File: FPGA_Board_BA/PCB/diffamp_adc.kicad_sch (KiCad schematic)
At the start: 12 parts, among them U1601 1819_IS8

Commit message: work
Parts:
- renumbered C1601 to C28, C1604 to C29, C1606 to C30, C1607 to C31, C1608 to C32, R1601 to R16, R1603 to R17, R1605 to R18, R1607 to R19, R1608 to R20, R1609 to R21, U1601 to U8

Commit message: 18.11 Bib Session
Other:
- moved on the sheet: C32, U8C
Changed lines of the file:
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@@
 	)
 	(junction
-		(at 199.39 90.17)
+		(at 218.44 90.17)
 		(diameter 0)
 		(color 0 0 0 0)
@@
 	)
 	(junction
-		(at 199.39 115.57)
+		(at 218.44 115.57)
 		(diameter 0)
 		(color 0 0 0 0)
@@
 	(wire
 		(pts
-			(xy 204.47 93.98) (xy 204.47 90.17)
+			(xy 223.52 93.98) (xy 223.52 90.17)
 		)
 		(stroke
@@
 	(wire
 		(pts
-			(xy 199.39 115.57) (xy 199.39 119.38)
+			(xy 218.44 115.57) (xy 218.44 119.38)
 		)
 		(stroke
@@
 	(wire
 		(pts
-			(xy 194.31 105.41) (xy 194.31 115.57)
+			(xy 213.36 105.41) (xy 213.36 115.57)
 		)
 		(stroke
@@
 	(wire
 		(pts
-			(xy 199.39 115.57) (xy 204.47 115.57)
+			(xy 218.44 115.57) (xy 223.52 115.57)
 		)
 		(stroke
@@
 	(wire
 		(pts
-			(xy 194.31 90.17) (xy 194.31 97.79)
+			(xy 213.36 90.17) (xy 213.36 97.79)
 		)
 		(stroke
@@
 	(wire
 		(pts
-			(xy 199.39 86.36) (xy 199.39 90.17)
+			(xy 218.44 86.36) (xy 218.44 90.17)
 		)
 		(stroke
@@
 	(wire
 		(pts
-			(xy 199.39 90.17) (xy 194.31 90.17)
+			(xy 218.44 90.17) (xy 213.36 90.17)
 		)
 		(stroke
@@
 	(wire
 		(pts
-			(xy 204.47 90.17) (xy 199.39 90.17)
+			(xy 223.52 90.17) (xy 218.44 90.17)
 		)
 		(stroke
@@
 	(wire
 		(pts
-			(xy 204.47 109.22) (xy 204.47 115.57)
+			(xy 223.52 109.22) (xy 223.52 115.57)
 		)
 		(stroke
@@
 	(wire
 		(pts
-			(xy 194.31 115.57) (xy 199.39 115.57)
+			(xy 213.36 115.57) (xy 218.44 115.57)
 		)
 		(stroke
@@
 	(symbol
 		(lib_id "power:+5VA")
-		(at 199.39 86.36 0)
+		(at 218.44 86.36 0)
 		(unit 1)
 		(exclude_from_sim no)
@@
 		(fields_autoplaced yes)
 		(property "Reference" "#PWR036"
-			(at 199.39 90.17 0)
+			(at 218.44 90.17 0)
 			(effects
 				(font
@@
 		)
 		(property "Value" "+5VA"
-			(at 199.39 81.28 0)
+			(at 218.44 81.28 0)
 			(effects
 				(font
@@
 		)
 		(property "Footprint" ""
-			(at 199.39 86.36 0)
+			(at 218.44 86.36 0)
 			(effects
 				(font
@@
 		)
 		(property "Datasheet" ""
-			(at 199.39 86.36 0)
+			(at 218.44 86.36 0)
 			(effects
 				(font
@@
 		)
 		(property "Description" "Power symbol creates a global label with name \"+5VA\""
-			(at 199.39 86.36 0)
+			(at 218.44 86.36 0)
 			(effects
 				(font
@@
 	(symbol
 		(lib_id "MYLIB_Misc:LT1819_IS8")
-		(at 198.12 101.6 0)
+		(at 217.17 101.6 0)
 		(mirror y)
 		(unit 3)
@@
 		(fields_autoplaced yes)
 		(property "Reference" "U8"
-			(at 205.74 100.3299 0)
+			(at 224.79 100.3299 0)
 			(effects
 				(font
@@
 		)
 		(property "Value" "1819_IS8"
-			(at 205.74 102.8699 0)
+			(at 224.79 102.8699 0)
 			(effects
 				(font
@@
 		)
 		(property "Footprint" "MYLIB_Misc:LT1819"
-			(at 197.866 88.646 0)
+			(at 216.916 88.646 0)
 			(effects
 				(font
@@
 		)
 		(property "Datasheet" "https://www.analog.com/media/en/technical-documentation/data-sheets/18189fb.pdf"
-			(at 198.628 84.074 0)
+			(at 217.678 84.074 0)
 			(effects
 				(font
@@
 		)
 		(property "Description" "ual wide bandwidth, high slew rate, low noise and distortion operational amplifi ers with excellent DC performance"
-			(at 198.374 86.106 0)
+			(at 217.424 86.106 0)
 			(effects
 				(font
@@
 	(symbol
 		(lib_id "WLIB_C:100n_0603")
-		(at 194.31 101.6 0)
+		(at 213.36 101.6 0)
 		(mirror y)
 		(unit 1)
@@
 		(dnp no)
 		(property "Reference" "C32"
-			(at 190.5 100.3299 0)
+			(at 209.55 100.3299 0)
 			(effects
 				(font
@@
 		)
 		(property "Value" "100n_0603"
-			(at 190.5 102.8699 0)
+			(at 209.55 102.8699 0)
 			(effects
 				(font
@@
 		)
 		(property "Footprint" "WLIB_Capacitor:C_0603"
-			(at 194.31 87.63 0)
+			(at 213.36 87.63 0)
 			(effects
 				(font
@@
 		)
 		(property "Datasheet" "https://www.farnell.com/datasheets/2860632.pdf"
-			(at 194.0052 80.01 0)
+			(at 213.0552 80.01 0)
 			(effects
 				(font
@@
 		)
 		(property "Description" "Unpolarized capacitor SMD MLCC"
-			(at 194.31 101.6 0)
+			(at 213.36 101.6 0)
 			(effects
 				(font
@@
 		)
 		(property "FARNELL" "1759037"
-			(at 194.0052 85.09 0)
+			(at 213.0552 85.09 0)
 			(effects
 				(font
@@
 		)
 		(property "VDC" "25V"
-			(at 194.0052 82.55 0)
+			(at 213.0552 82.55 0)
 			(effects
 				(font
@@
 		)
 		(property "JLCPCB" "C2762593"
-			(at 194.31 90.17 0)
+			(at 213.36 90.17 0)
 			(effects
 				(font
@@
 	(symbol
 		(lib_id "power:GND")
-		(at 199.39 119.38 0)
+		(at 218.44 119.38 0)
 		(unit 1)
 		(exclude_from_sim no)
@@
 		(fields_autoplaced yes)
 		(property "Reference" "#PWR037"
-			(at 199.39 125.73 0)
+			(at 218.44 125.73 0)
 			(effects
 				(font
@@
 		)
 		(property "Value" "GND"
-			(at 199.39 124.46 0)
+			(at 218.44 124.46 0)
 			(effects
 				(font
@@
 		)
 		(property "Footprint" ""
-			(at 199.39 119.38 0)
+			(at 218.44 119.38 0)
 			(effects
 				(font
@@
 		)
 		(property "Datasheet" ""
-			(at 199.39 119.38 0)
+			(at 218.44 119.38 0)
 			(effects
 				(font
@@
 		)
 		(property "Description" "Power symbol creates a global label with name \"GND\" , ground"
-			(at 199.39 119.38 0)
+			(at 218.44 119.38 0)
 			(effects
 				(font

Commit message: 22.11
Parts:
- added R206, R208: 9k1_0603, Resistor_SMD:R_0603_1608Metric, symbol WLIB_R:9k1_0603
- added R207: 1k_0603, Resistor_SMD:R_0603_1608Metric, symbol WLIB_R:1k_0603
- renumbered R17 to R10, R18 to R11, R19 to R12, R20 to R13, R21 to R14, R16 to R9, U8 to U4
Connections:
- net +5VA: no longer R14.2
- net Analog: now also R207.1; no longer R13.2, U4.3 (+)
- net GND: now also R206.2, R208.2
- new net: R13.2, R206.1, R207.2, R208.1, U4.3 (+)
- new net REFOUT_1: R14.2
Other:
- note added: "ADC Reference is 4.096V Vout = V * R1 / (R1 + R2) 4.096V = 5V * R1 / (R1 + R2) 0.8192 = R1 / (R1 + R2) 0.8192 * R1 + 0.8192 * R2 = R1 0.1808 * R1 = 0.8192 * R2 R1 / R2 = 4.53097 R1 := 9.1k || 9.1k = 4.55k R2 = 1k R1/R2 = 4.55 Vout_max = 5V * 4.55 / 5.55 = 4.099V -> very little saturation"
- note added: "R1"
- note added: "R2"

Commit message: exported stuff
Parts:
- renumbered R206 to R15, R207 to R16, R208 to R17
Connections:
- net REFOUT_1 renamed REFOUT_M
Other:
- note added: "Single ended to differential for CHB"

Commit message: schematic fixes after Leo Meeting
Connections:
- net at R15.1, R16.2, R17.1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: no longer R13.2
- net at R9.2, U4.1, U4.2 (-): now also R13.2
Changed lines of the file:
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@@
 	)
 	(junction
-		(at 154.94 73.66)
+		(at 138.43 85.09)
 		(diameter 0)
 		(color 0 0 0 0)
@@
 	(wire
 		(pts
-			(xy 129.54 73.66) (xy 154.94 73.66)
-		)
-		(stroke
-			(width 0)
-			(type default)
-		)
-	)
-	(wire
-		(pts
 			(xy 127 143.51) (xy 135.89 143.51)
 		)
@@
 	(wire
 		(pts
+			(xy 138.43 85.09) (xy 154.94 85.09)
+		)
+		(stroke
+			(width 0)
+			(type default)
+		)
+	)
+	(wire
+		(pts
 			(xy 110.49 90.17) (xy 110.49 76.2)
 		)
@@
 	(wire
 		(pts
-			(xy 154.94 73.66) (xy 154.94 109.22)
+			(xy 138.43 85.09) (xy 138.43 90.17)
 		)
 		(stroke
@@
 	(wire
 		(pts
-			(xy 138.43 78.74) (xy 138.43 90.17)
+			(xy 138.43 78.74) (xy 138.43 85.09)
 		)
 		(stroke
@@
 	(wire
 		(pts
+			(xy 154.94 109.22) (xy 154.94 85.09)
+		)
+		(stroke
+			(width 0)
+			(type default)
+		)
+	)
+	(wire
+		(pts
 			(xy 110.49 100.33) (xy 116.84 100.33)
 		)
@@
 	(wire
 		(pts
-			(xy 154.94 73.66) (xy 175.26 73.66)
-		)
-		(stroke
+			(xy 129.54 73.66) (xy 175.26 73.66)
+		)
+		(stroke

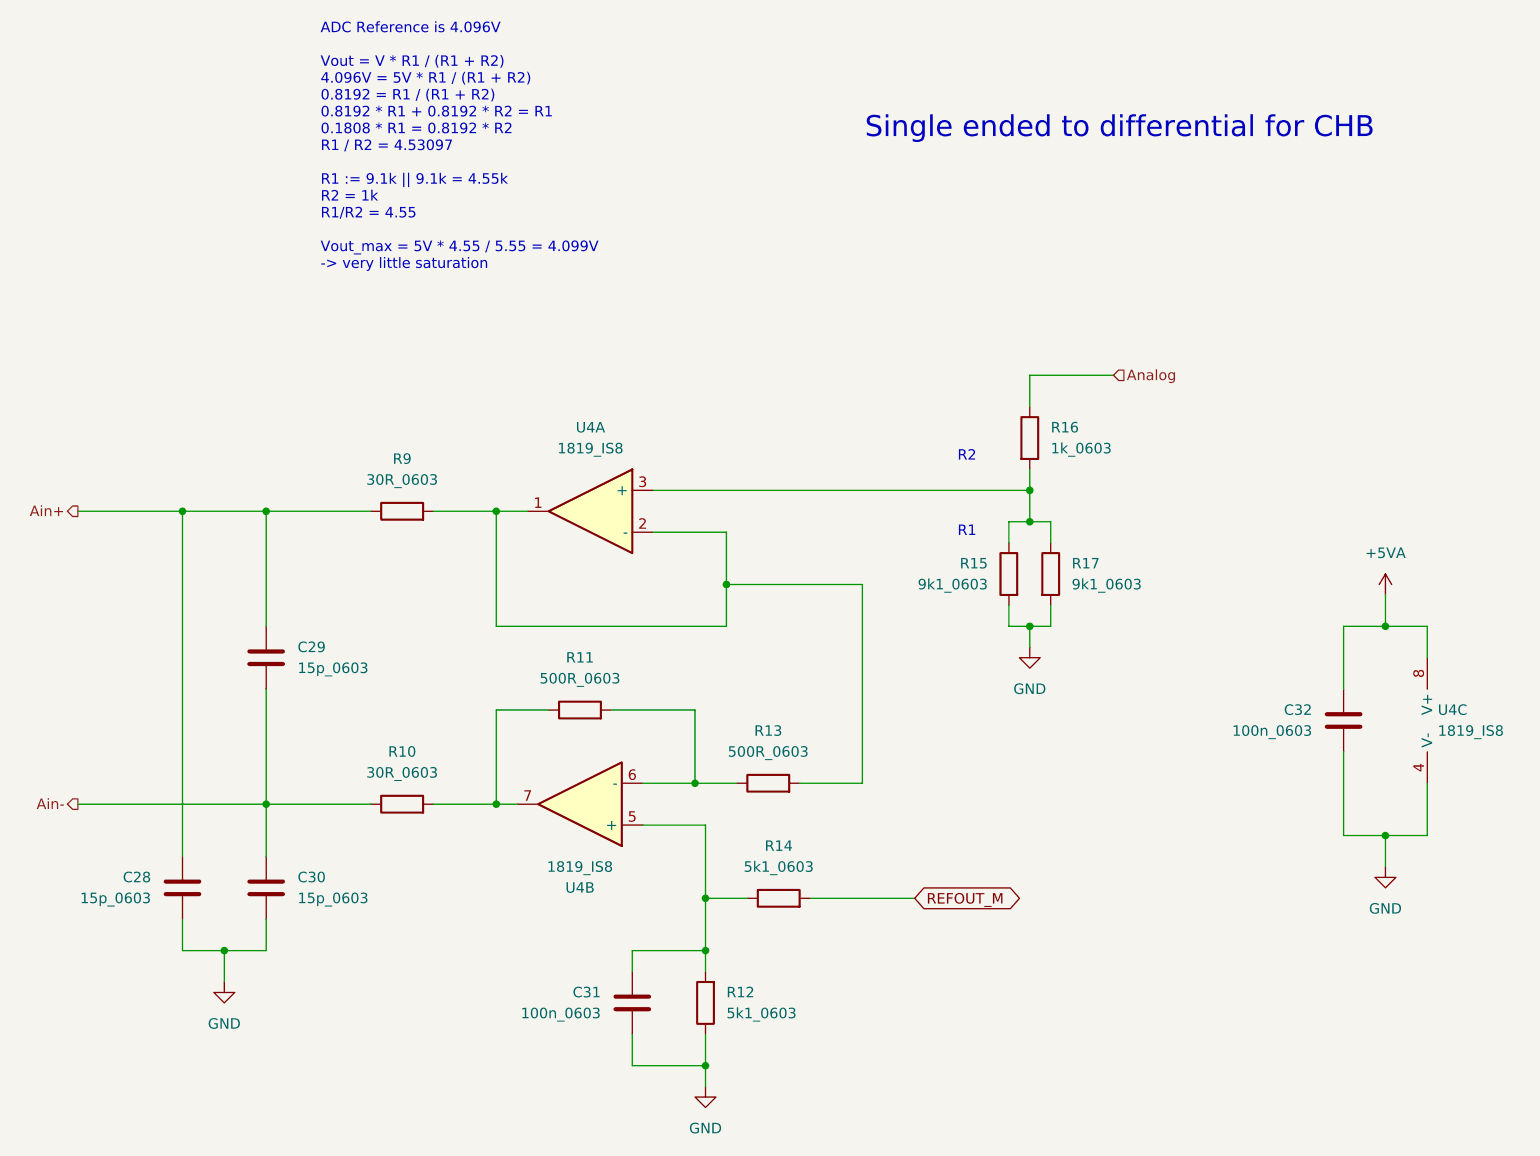
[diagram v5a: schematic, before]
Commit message: component placement with new concept is ready
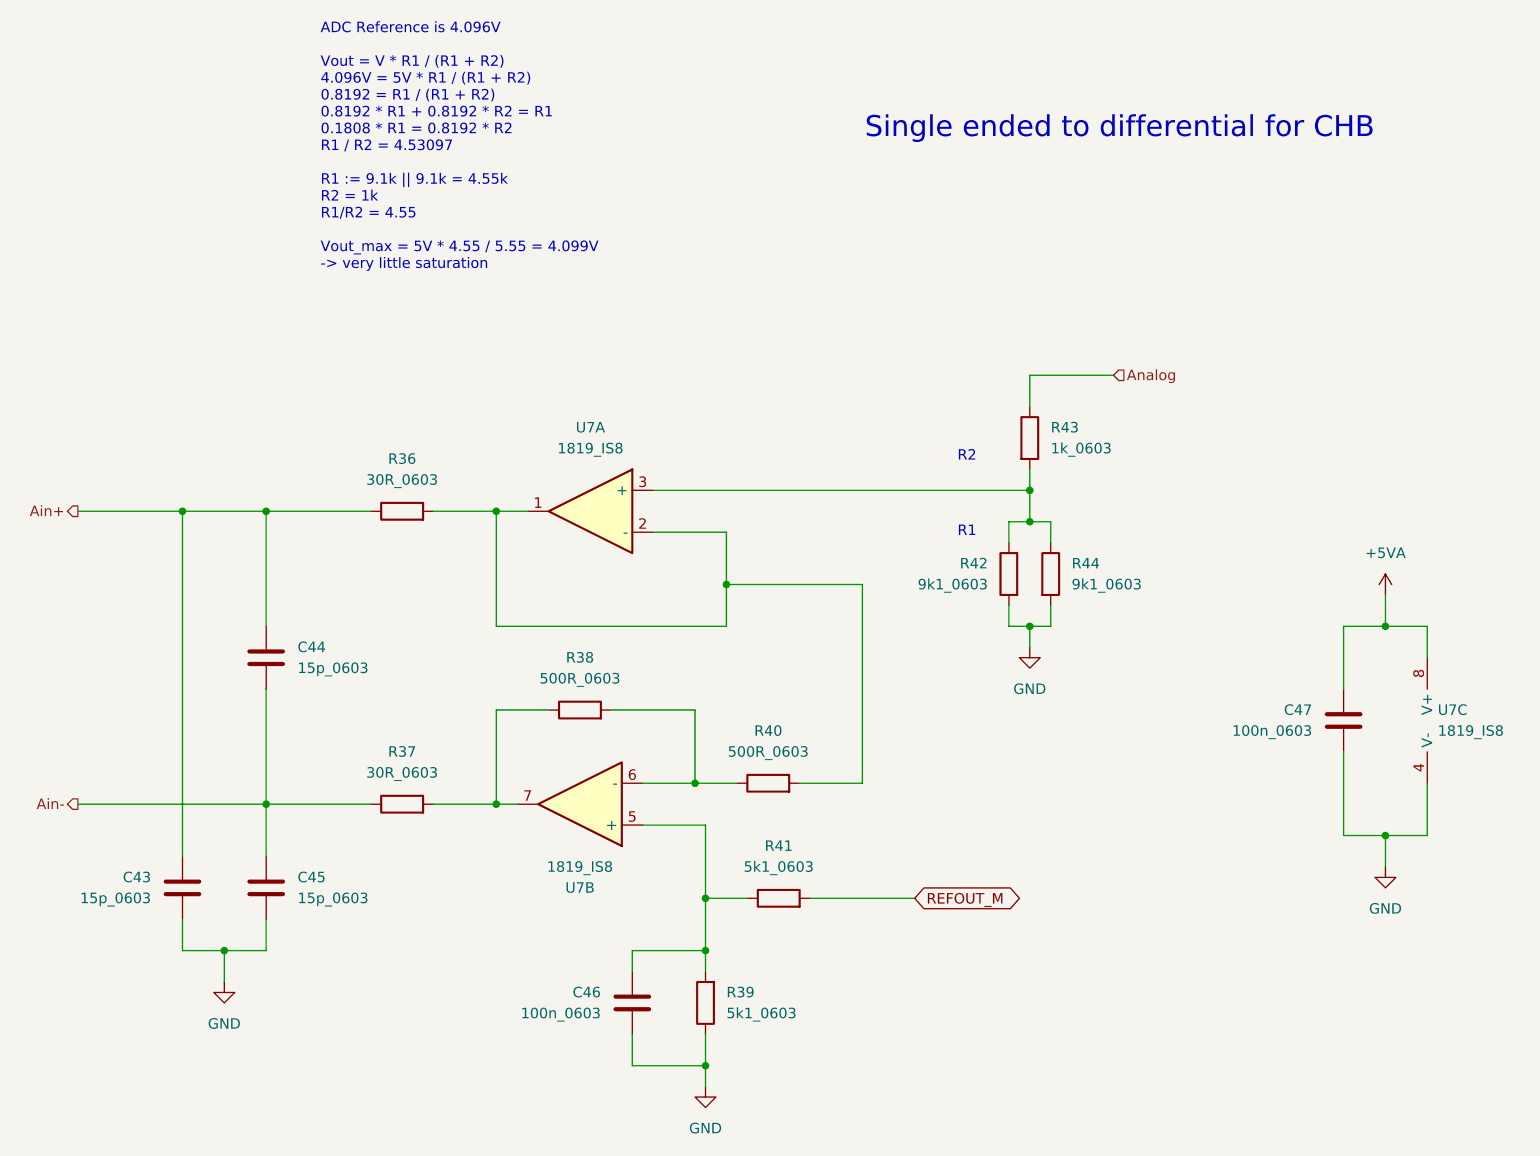
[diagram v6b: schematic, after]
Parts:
- renumbered C28 to C43, C29 to C44, C30 to C45, C31 to C46, C32 to C47, R9 to R36, R10 to R37, R11 to R38, R12 to R39, R13 to R40, R14 to R41, R15 to R42, R16 to R43, R17 to R44, U4 to U7
